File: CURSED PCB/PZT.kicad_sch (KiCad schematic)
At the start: 6 parts, among them J4 2 Wire Block for PZT, U12 AD5761BRUZ

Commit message: updated schematic
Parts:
- added C33: 100nF, Capacitor_SMD:C_0805_2012Metric_Pad1.18x1.45mm_HandSolder, symbol PCM_Capacitor_US_AKL:C_0201
- added C34: 10uF, Capacitor_SMD:C_0805_2012Metric_Pad1.18x1.45mm_HandSolder, symbol PCM_Capacitor_US_AKL:C_0201
- added R3: Unkown, Resistor_SMD:R_0805_2012Metric_Pad1.20x1.40mm_HandSolder, symbol Device:R_US
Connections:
- net GND: now also C33.1, C34.1
- net at U12.7 (VOUT): now also R3.1; no longer J4.1
- net PZT_BOOST_out renamed +24V
- new net: C33.2, C34.2, J4.1, R3.2
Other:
- note added: "Acceptable Voltage Flucation of +-0.5V Low pass introduced to force the acceptable voltage range Reistior to be found experimentally Proof in google sheets labbeled "Experimental & PCB Data Setup Master" under Photodiode Experimental Data, Requirments & Comparison of PZT & Comparison of PZT to Generated Current in Payload GOogle drive"
- note removed: "24V"

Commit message: schematic changes
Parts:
- removed J4: 2 Wire Block for PZT, 691137710002:691137710002, symbol 691137710002:691137710002
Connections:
- net DAC_RESET: now reaches U12.3 (~{RESET})
- net PZT: now reaches C33.2, C34.2, R3.2
- no-connect marks 4 -> 3
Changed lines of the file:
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@@
-	)
-	(no_connect
-		(at 95.25 62.23)
 	)
 	(no_connect
@@
 	(wire
 		(pts
-			(xy 95.25 132.08) (xy 95.25 137.16)
-		)
-		(stroke
-			(width 0)
-			(type default)
-		)
-	)
-	(wire
-		(pts
 			(xy 72.39 92.71) (xy 74.93 92.71)
 		)
@@
 		(pts
 			(xy 87.63 57.15) (xy 87.63 62.23)
+		)
+		(stroke
+			(width 0)
+			(type default)
+		)
+	)
+	(wire
+		(pts
+			(xy 95.25 62.23) (xy 99.06 62.23)
 		)
 		(stroke
@@
 		(shape input)
 		(at 85.09 53.34 0)
+		(effects
+			(font
+				(size 1.27 1.27)
+			)
+			(justify left)
+		)
+	)
+	(hierarchical_label "DAC_RESET"
+		(shape input)
+		(at 99.06 62.23 0)
+		(effects
+			(font
+				(size 1.27 1.27)
+			)
+			(justify left)
+		)
+	)
+	(hierarchical_label "PZT"
+		(shape input)
+		(at 95.25 129.54 0)
 		(effects
 			(font
@@
 	)
 	(symbol
-		(lib_id "power:GND")
-		(at 95.25 137.16 0)
-		(unit 1)
-		(exclude_from_sim no)
-		(in_bom yes)
-		(on_board yes)
-		(dnp no)
-		(fields_autoplaced yes)
-		(property "Reference" "#PWR010"
-			(at 95.25 143.51 0)
-			(effects
-				(font
-					(size 1.27 1.27)
-				)
-				(hide yes)
-			)
-		)
-		(property "Value" "GND"
-			(at 95.25 142.24 0)
-			(effects
-				(font
-					(size 1.27 1.27)
-				)
-			)
-		)
-		(property "Footprint" ""
-			(at 95.25 137.16 0)
-			(effects
-				(font
-					(size 1.27 1.27)
-				)
-				(hide yes)
-			)
-		)
-		(property "Datasheet" ""
-			(at 95.25 137.16 0)
-			(effects
-				(font
-					(size 1.27 1.27)
-				)
-				(hide yes)
-			)
-		)
-		(property "Description" "Power symbol creates a global label with name \"GND\" , ground"
-			(at 95.25 137.16 0)
-			(effects
-				(font
-					(size 1.27 1.27)
-				)
-				(hide yes)
-			)
-		)
-		(pin "1"
-		)
-		(instances
-			(project "sensor_1"
-				(path "/9fb1a86f-679c-4b88-9ed1-932f4f414580/0db50404-6532-4147-817b-c9e90e06de0c"
-					(reference "#PWR010")
-					(unit 1)
-				)
-			)
-		)
-	)
-	(symbol
 		(lib_id "AD5761BRUZ:AD5761BRUZ")
 		(at 82.55 77.47 270)
@@
 					(unit 1)
 				)
-			)
-		)
-	)
-	(symbol
-		(lib_id "691137710002:691137710002")
-		(at 100.33 132.08 270)
-		(unit 1)
-		(exclude_from_sim no)
-		(in_bom yes)
-		(on_board yes)
-		(dnp no)
-		(property "Reference" "J4"
-			(at 101.6 129.5399 90)
-			(effects
-				(font
-					(size 1.27 1.27)
-				)
-				(justify left)
-			)
-		)
-		(property "Value" "2 Wire Block for PZT"
-			(at 101.6 132.08 90)
-			(effects
-				(font
-					(size 1.27 1.27)
-				)
-				(justify left)
-			)
-		)
-		(property "Footprint" "691137710002:691137710002"
-			(at 100.33 132.08 0)
-			(effects
-				(font
-					(size 1.27 1.27)
-				)
-				(justify bottom)
-				(hide yes)
-			)
-		)
-		(property "Datasheet" "https://thin01mstroc282prod.dxcloud.episerver.net/globalassets/items/p/pa/pa2/pa25few/ctn014120-s01.pdf?v=0116015302?v=2026-01-16-13-53-02"
-			(at 100.33 132.08 0)
-			(effects
-				(font
-					(size 1.27 1.27)
-				)
-				(hide yes)
-			)
-		)
-		(property "Description" ""
-			(at 100.33 132.08 0)
-			(effects
-				(font
-					(size 1.27 1.27)
-				)
-				(hide yes)
-			)
-		)
-		(property "DigiKey_Part_Number" "732-10955-ND"
-			(at 100.33 132.08 0)
-			(effects
-				(font
-					(size 1.27 1.27)
-				)
-				(justify bottom)
-				(hide yes)
-			)
-		)
-		(property "SnapEDA_Link" "https://www.snapeda.com/parts/691137710002/W%25C3%25BCrth+Elektronik+Midcom/view-part/?ref=snap"
-			(at 100.33 132.08 0)
-			(effects
-				(font
-					(size 1.27 1.27)
-				)
-				(justify bottom)
-				(hide yes)
-			)
-		)
-		(property "Description_1" "2 Position Wire to Board Terminal Block Horizontal with Board 0.197 (5.00mm) Through Hole"
-			(at 100.33 132.08 0)
-			(effects
-				(font
-					(size 1.27 1.27)
-				)
-				(justify bottom)
-				(hide yes)
-			)
-		)
-		(property "MF" "Würth Elektronik"
-			(at 100.33 132.08 0)
-			(effects
-				(font
-					(size 1.27 1.27)
-				)
-				(justify bottom)
-				(hide yes)
-			)
-		)
-		(property "Package" "None"
-			(at 100.33 132.08 0)
-			(effects
-				(font
-					(size 1.27 1.27)
-				)
-				(justify bottom)
-				(hide yes)
-			)
-		)
-		(property "Check_prices" "https://www.snapeda.com/parts/691137710002/W%25C3%25BCrth+Elektronik+Midcom/view-part/?ref=eda"
-			(at 100.33 132.08 0)
-			(effects
-				(font
-					(size 1.27 1.27)
-				)
-				(justify bottom)
-				(hide yes)
-			)
-		)
-		(property "MP" "691137710002"
-			(at 100.33 132.08 0)
-			(effects
-				(font
-					(size 1.27 1.27)
-				)
-				(justify bottom)
-				(hide yes)
-			)
-		)
-		(pin "2"
-		)
-		(pin "1"
-		)
-		(instances
-			(project "sensor_1"
-				(path "/9fb1a86f-679c-4b88-9ed1-932f4f414580/0db50404-6532-4147-817b-c9e90e06de0c"
-					(reference "J4")
-					(unit 1)
-				)

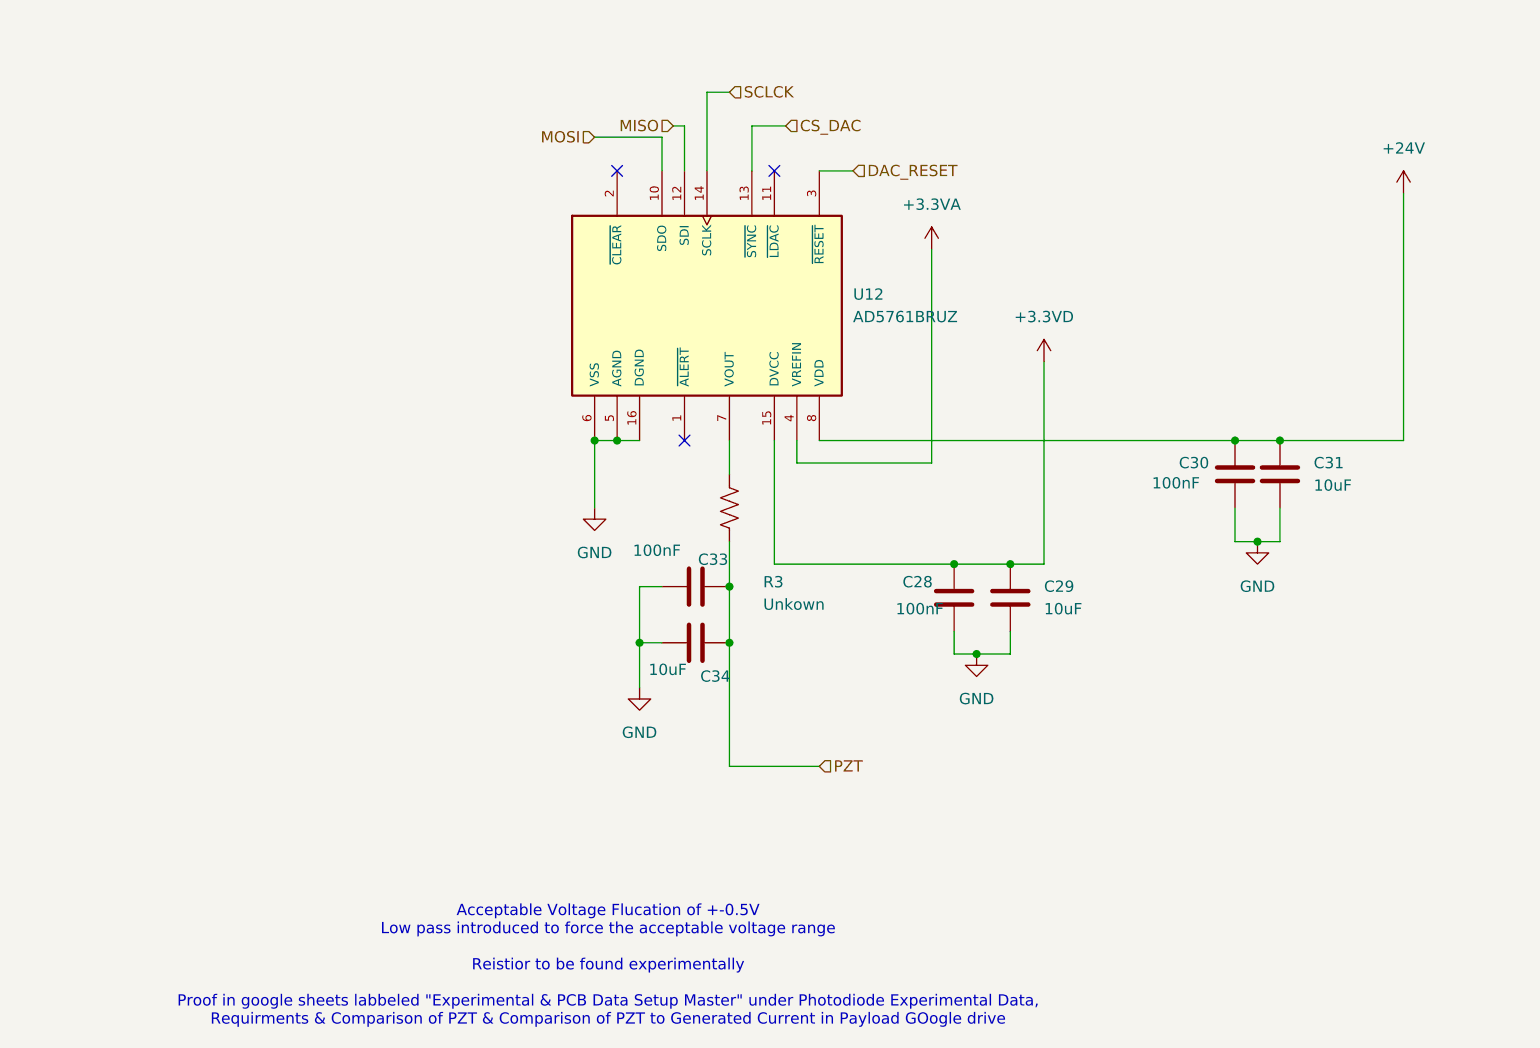
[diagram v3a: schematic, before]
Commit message: updates traces and footprints
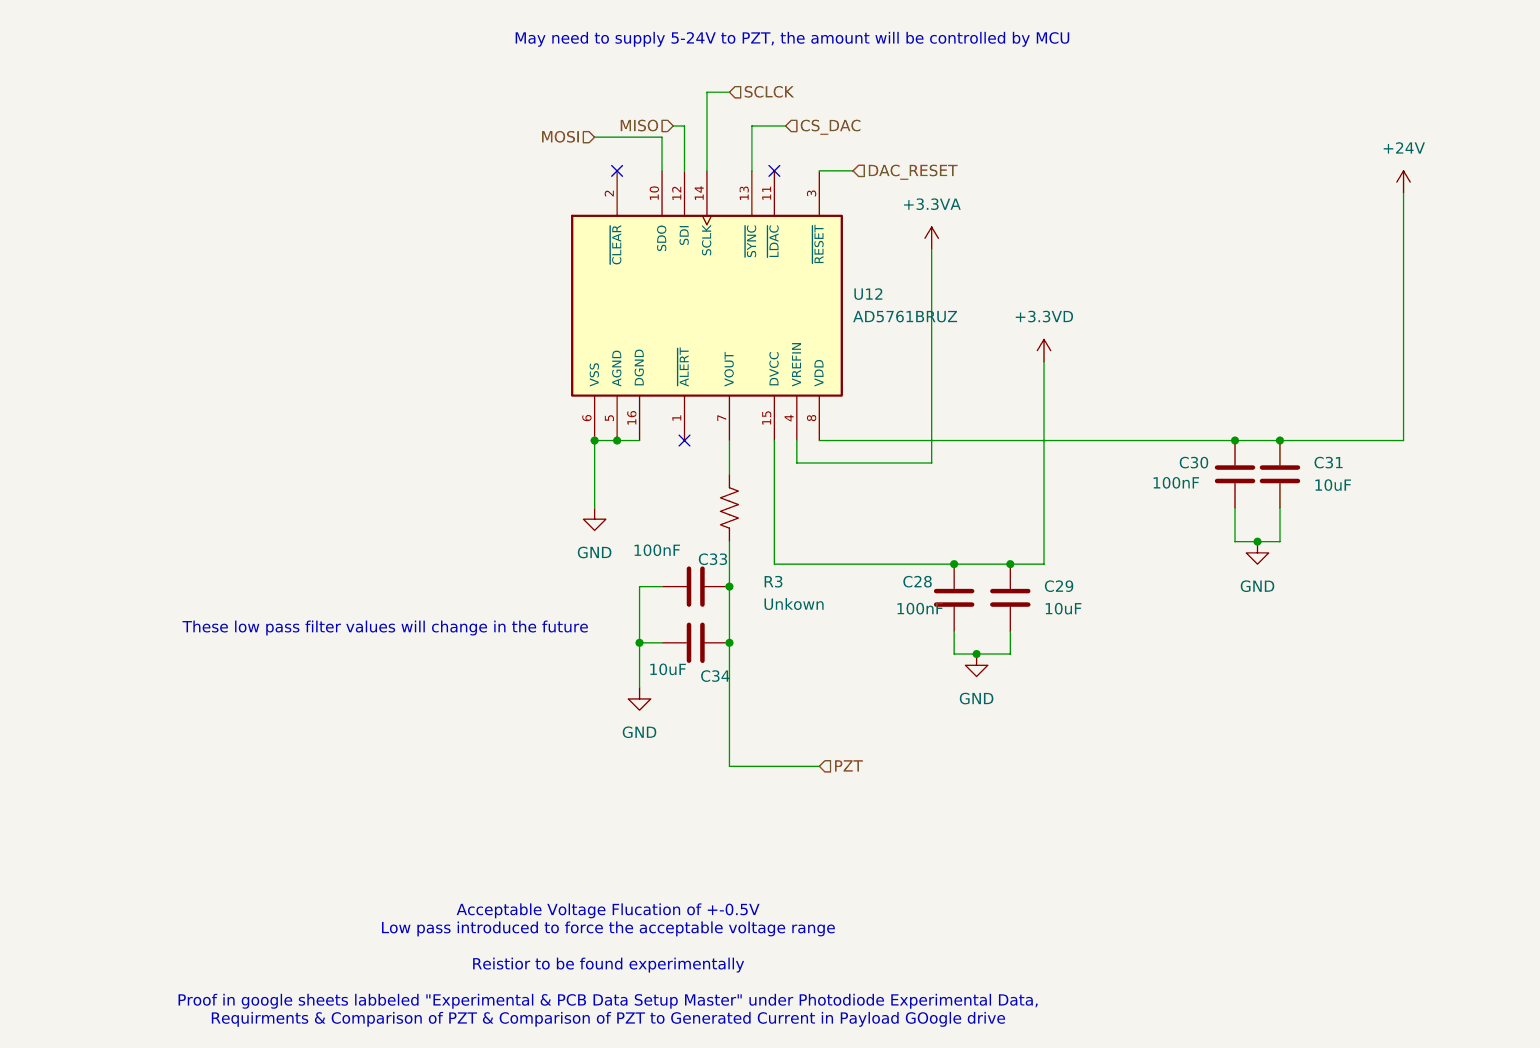
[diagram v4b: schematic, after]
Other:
- note added: "May need to supply 5-24V to PZT, the amount will be controlled by MCU"
- note added: "These low pass filter values will change in the future"
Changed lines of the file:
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@@
 	(generator_version "9.0")
 	(paper "A4")
+	(text "These low pass filter values will change in the future"
+		(exclude_from_sim no)
+		(at 46.228 114.046 0)
+		(effects
+			(font
+				(size 1.27 1.27)
+			)
+		)
+	)
+	(text "May need to supply 5-24V to PZT, the amount will be controlled by MCU"
+		(exclude_from_sim no)
+		(at 92.202 47.498 0)
+		(effects
+			(font
+				(size 1.27 1.27)
+			)
+		)
+	)
 	(text "Acceptable Voltage Flucation of +-0.5V \nLow pass introduced to force the acceptable voltage range\n\nReistior to be found experimentally \n\nProof in google sheets labbeled \"Experimental & PCB Data Setup Master\" under Photodiode Experimental Data, \nRequirments & Comparison of PZT & Comparison of PZT to Generated Current in Payload GOogle drive"
 		(exclude_from_sim no)

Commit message: Updated PDF and make schematic look more pretty
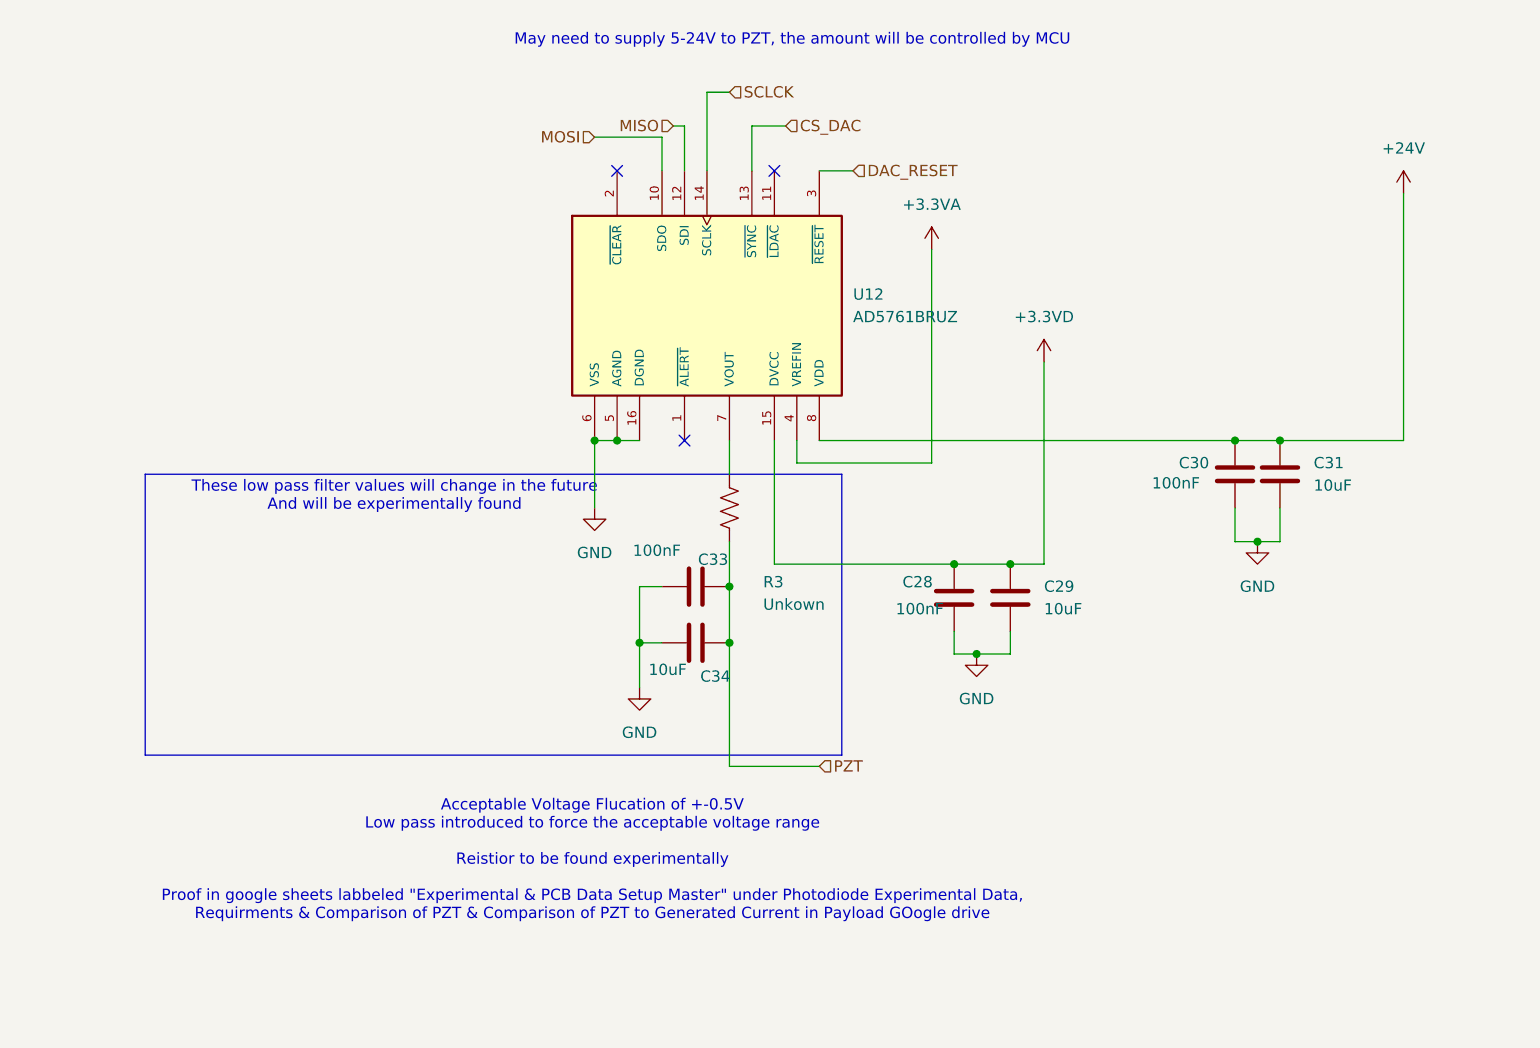
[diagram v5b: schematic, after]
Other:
- note added: "These low pass filter values will change in the future And will be experimentally found"
- note removed: "These low pass filter values will change in the future"
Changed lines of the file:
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@@
 	(generator_version "9.0")
 	(paper "A4")
-	(text "These low pass filter values will change in the future"
+	(rectangle
+		(start 19.05 96.52)
+		(end 97.79 128.27)
+		(stroke
+			(width 0)
+			(type default)
+		)
+		(fill
+			(type none)
+		)
+	)
+	(text "These low pass filter values will change in the future\nAnd will be experimentally found "
 		(exclude_from_sim no)
-		(at 46.228 114.046 0)
+		(at 47.244 99.06 0)
 		(effects
 			(font
@@
 	(text "Acceptable Voltage Flucation of +-0.5V \nLow pass introduced to force the acceptable voltage range\n\nReistior to be found experimentally \n\nProof in google sheets labbeled \"Experimental & PCB Data Setup Master\" under Photodiode Experimental Data, \nRequirments & Comparison of PZT & Comparison of PZT to Generated Current in Payload GOogle drive"
 		(exclude_from_sim no)
-		(at 71.374 152.146 0)
+		(at 69.596 140.208 0)
 		(effects
 			(font

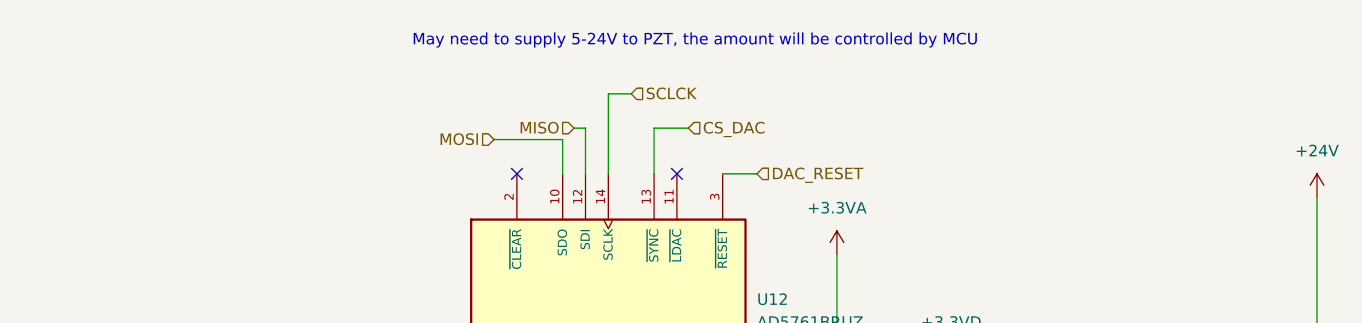
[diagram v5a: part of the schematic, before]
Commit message: Rewording schematic text
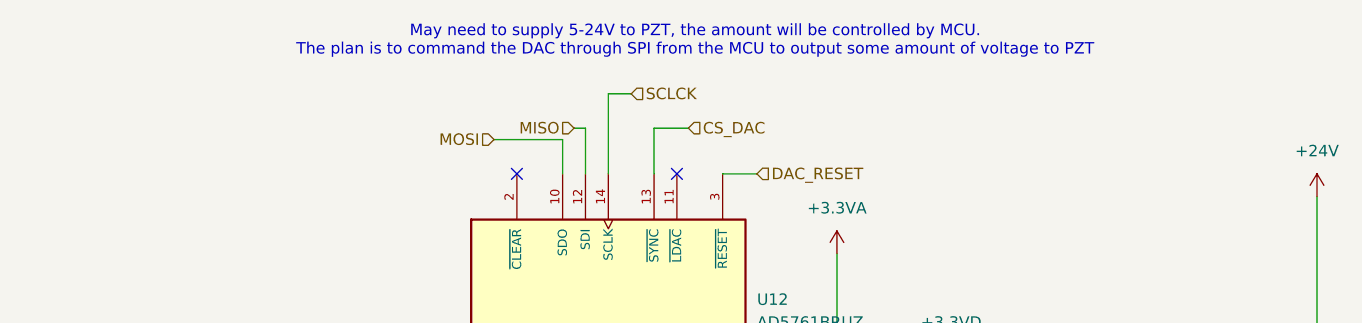
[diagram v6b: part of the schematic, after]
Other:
- note added: "May need to supply 5-24V to PZT, the amount will be controlled by MCU. The plan is to command the DAC through SPI from the MCU to output some amount of voltage to PZT"
- note removed: "May need to supply 5-24V to PZT, the amount will be controlled by MCU"
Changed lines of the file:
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@@
 		)
 	)
-	(text "May need to supply 5-24V to PZT, the amount will be controlled by MCU"
+	(text "May need to supply 5-24V to PZT, the amount will be controlled by MCU.\nThe plan is to command the DAC through SPI from the MCU to output some amount of voltage to PZT"
 		(exclude_from_sim no)
 		(at 92.202 47.498 0)
